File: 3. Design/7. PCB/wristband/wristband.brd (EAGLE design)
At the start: 160 x 100 mm, 4 parts, among them IC1 MPU-6050, IC2 MAX16150AUT+T, IC4 NRF24L01P-T, IC5 STM32F051K6U6

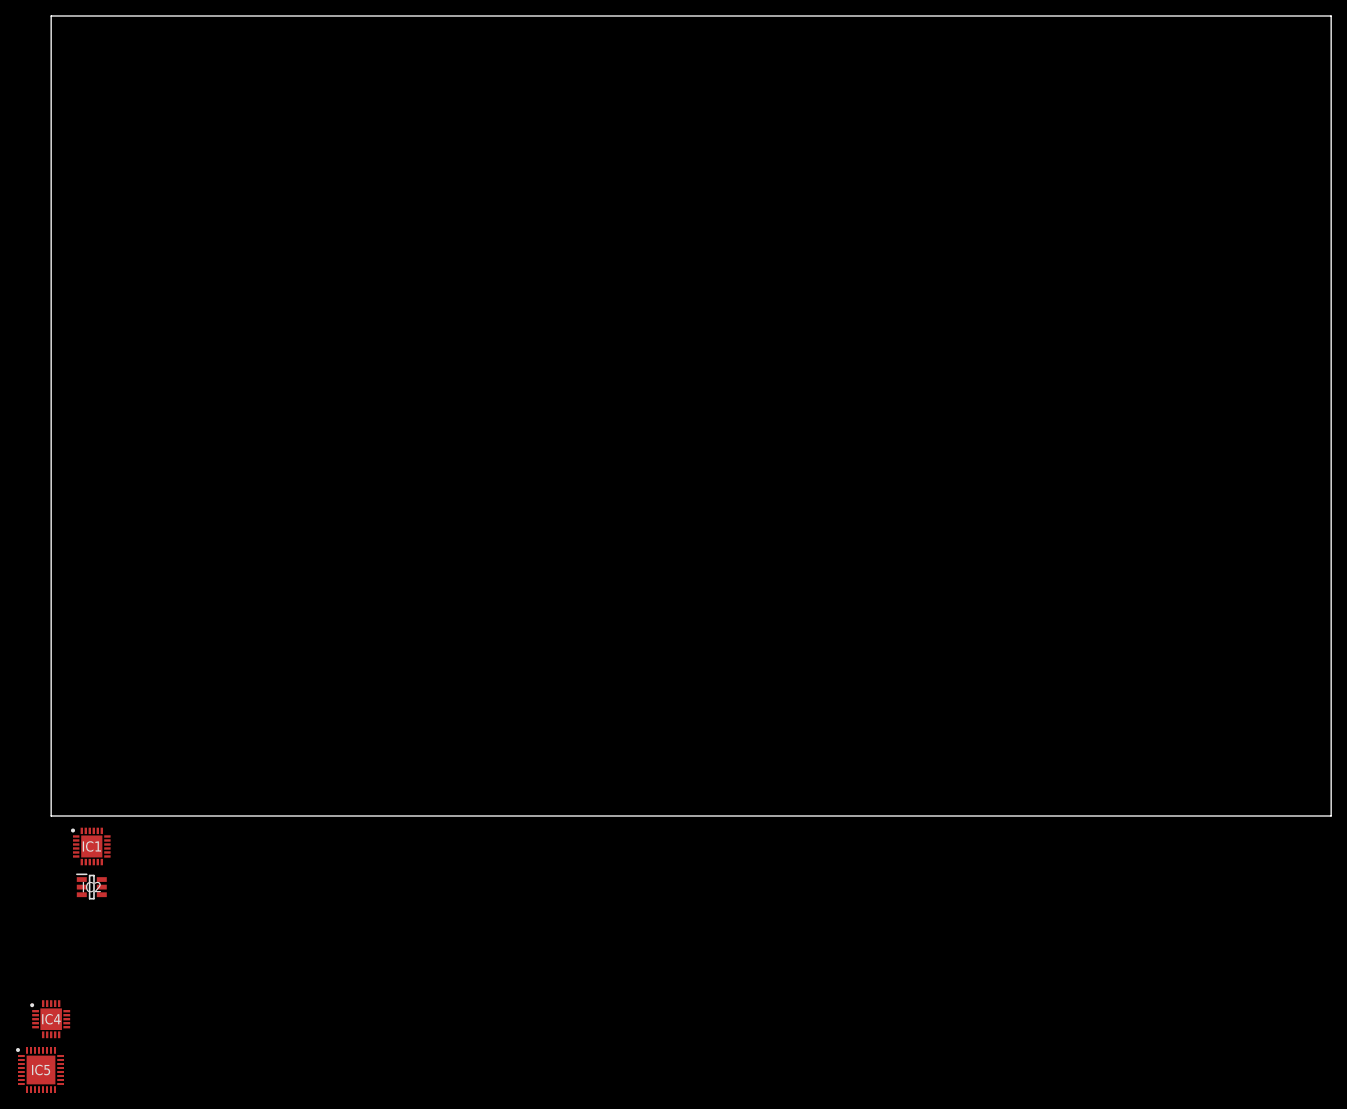
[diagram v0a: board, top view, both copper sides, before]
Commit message: ADD|UPDT: Added new antenna library files and initial nRF24L01-balun/filter-antenna interaction sketch
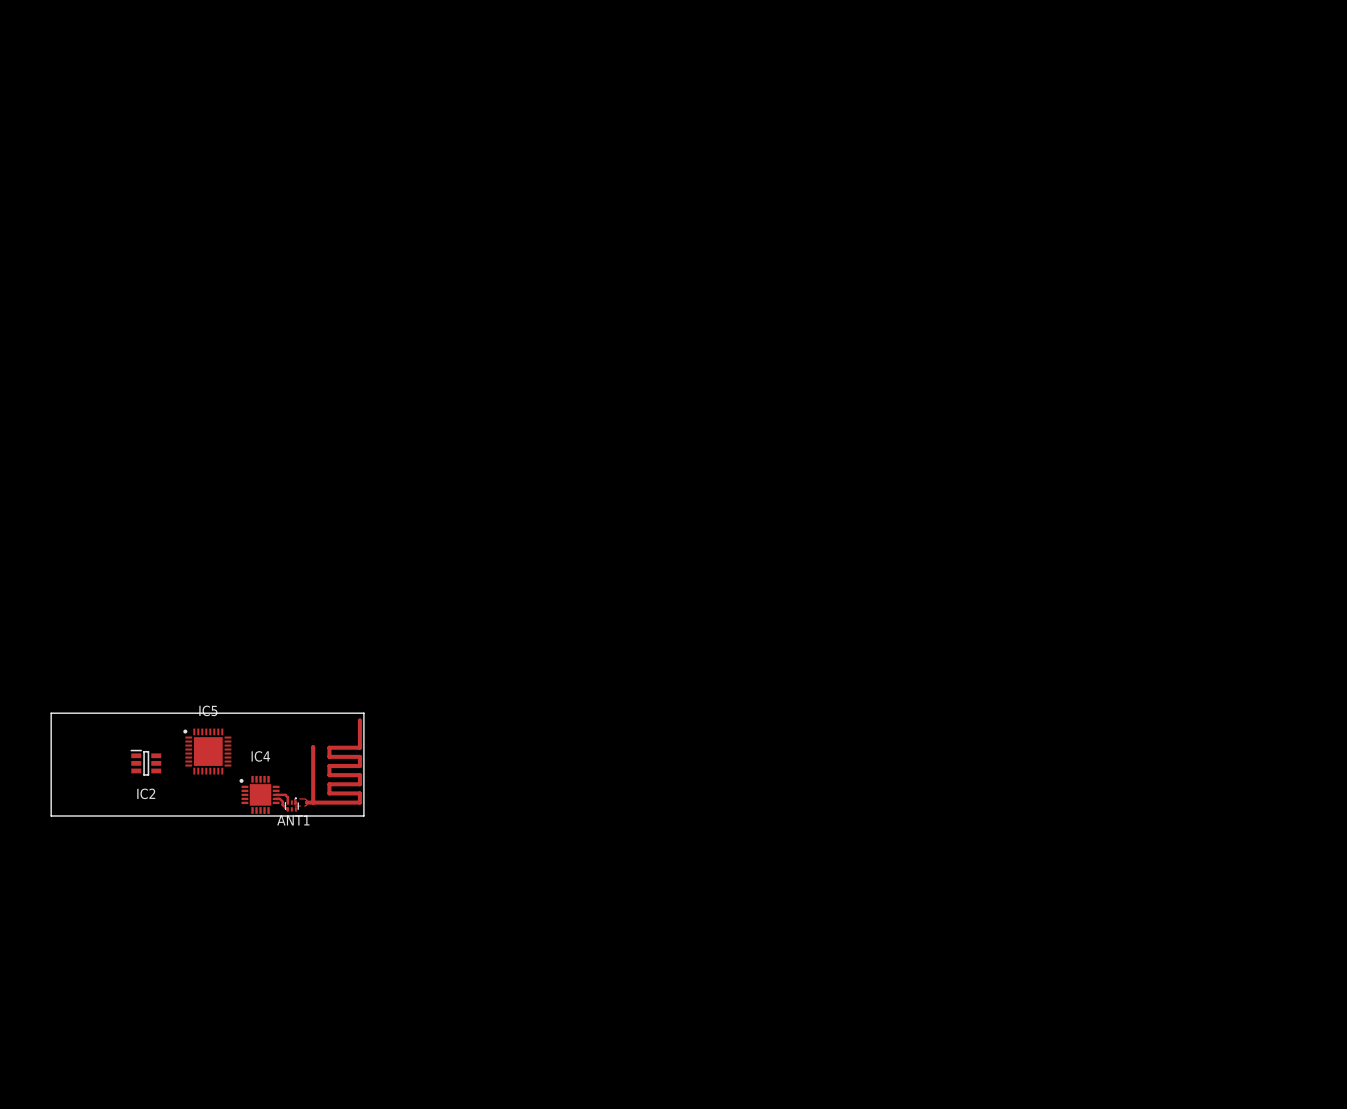
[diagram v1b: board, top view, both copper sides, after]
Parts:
- removed IC1: MPU-6050, MPU-6050:QFN50P400X400X95-25N
- added ANT1: 2450BM14A0002T, 2450BM14A0002T:2450BM14A0002T
- added U$2: MIFA-CYPRESS-2, MIFA:MIFA-CYPRESS-2
- moved IC5 45.0 mm to (19.6, 8.06)
- moved IC4 38.4 mm to (26.2, 2.64)
- moved IC2 16.9 mm to (11.9, 6.58)
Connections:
- new net ANT1: ANT1.4, IC4.12
- new net ANT2: ANT1.3, IC4.13
- new net GND: ANT1.2, U$2.GND
- new net N$1: ANT1.1, U$2.ANT
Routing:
- net ANT1: track 0.00 -> 2.24 mm
- net ANT2: track 0.00 -> 2.24 mm
- added copper zone on layer 1, net N$1
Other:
- board size 160 x 100 mm -> 39.1 x 12.9 mm
